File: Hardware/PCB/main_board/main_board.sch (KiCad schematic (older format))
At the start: 0 parts

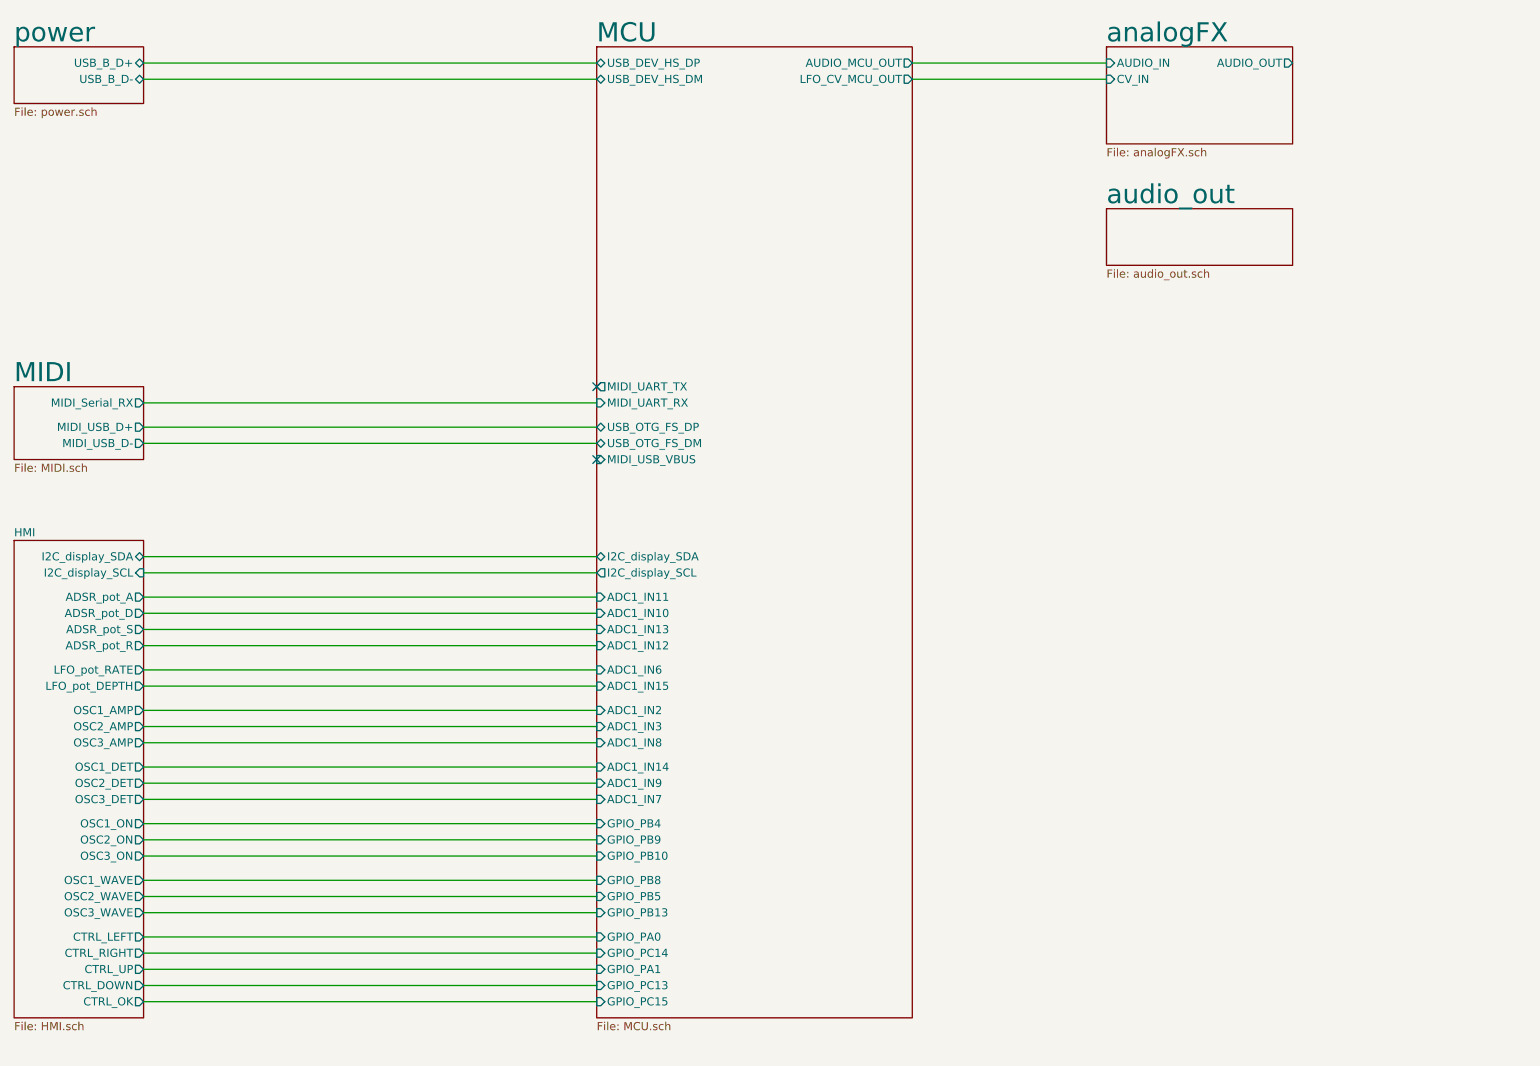
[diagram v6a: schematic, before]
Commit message: Add FX buffer and headphone amp to schematics
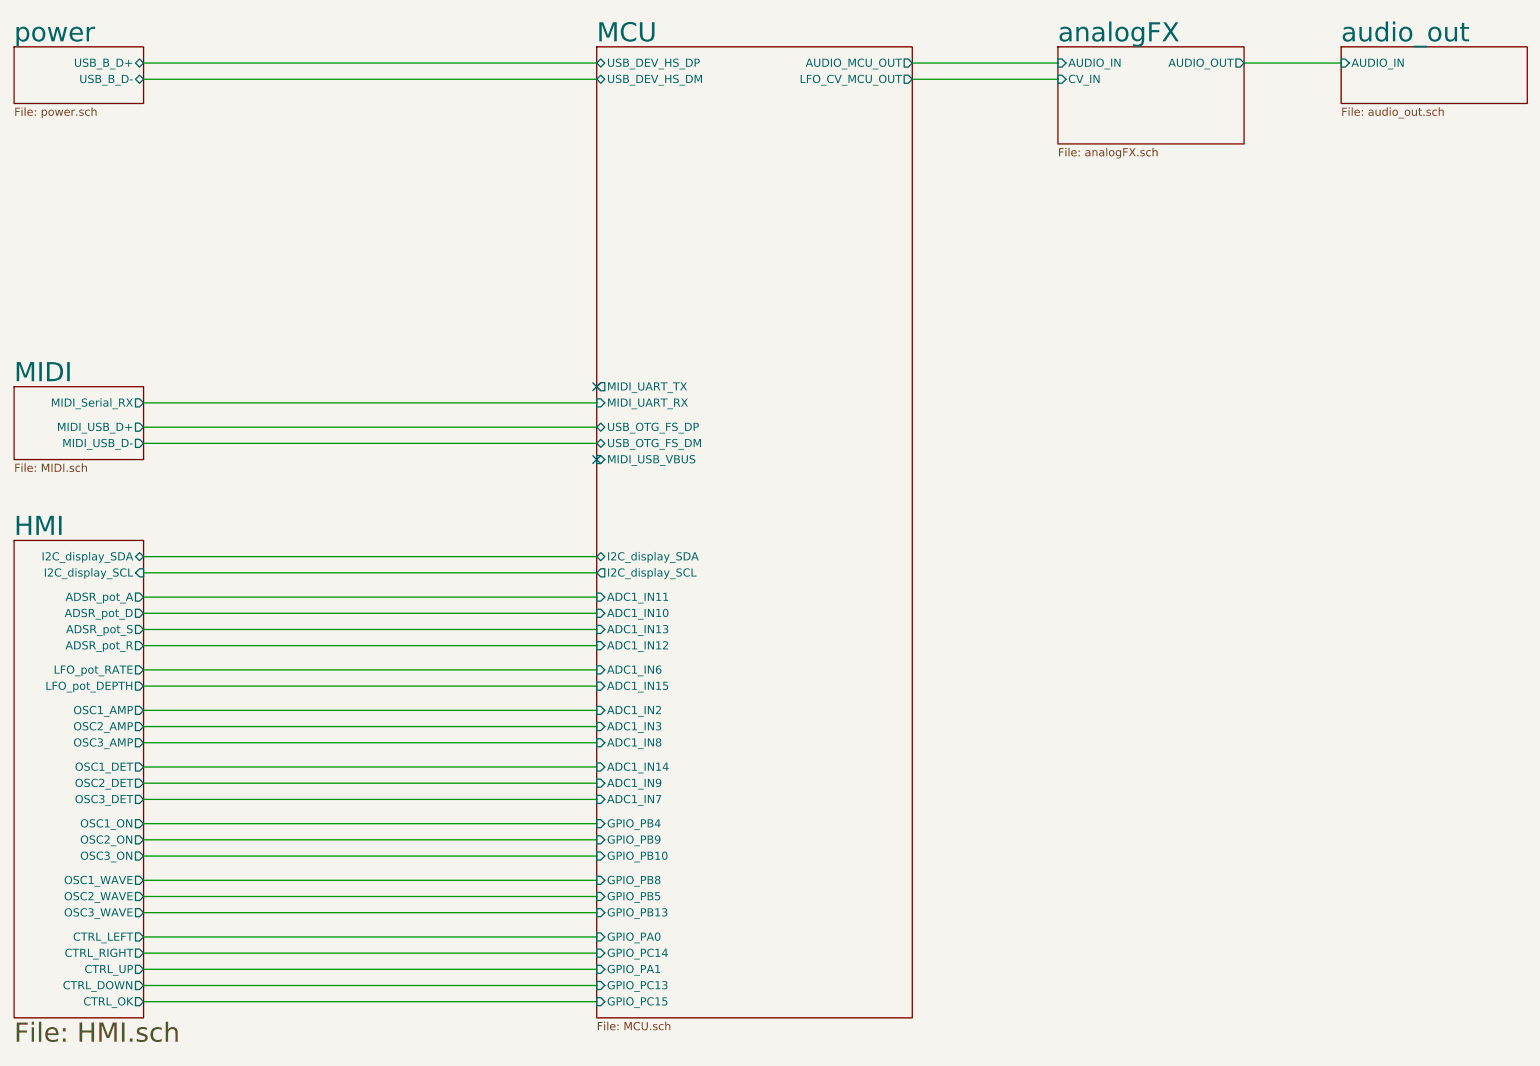
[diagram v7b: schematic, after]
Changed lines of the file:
@@
 $EndDescr
 Wire Wire Line
-	6750 1250 7950 1250
+	6750 1250 7650 1250
 Wire Wire Line
-	6750 1350 7950 1350
+	6750 1350 7650 1350
 $Sheet
 S 1200 3250 800  450
@@
 $EndSheet
 $Sheet
-S 7950 2150 1150 350
+S 9400 1150 1150 350
 U 5E68385C
 F0 "audio_out" 118
 F1 "audio_out.sch" 50
+F2 "AUDIO_IN" I L 9400 1250 50
 $EndSheet
 $Sheet
-S 7950 1150 1150 600
+S 7650 1150 1150 600
 U 5E632F77
 F0 "analogFX" 118
 F1 "analogFX.sch" 50
-F2 "AUDIO_OUT" O R 9100 1250 50
-F3 "CV_IN" I L 7950 1350 50
-F4 "AUDIO_IN" I L 7950 1250 50
+F2 "AUDIO_OUT" O R 8800 1250 50
+F3 "CV_IN" I L 7650 1350 50
+F4 "AUDIO_IN" I L 7650 1250 50
 $EndSheet
 $Sheet
 S 1200 4200 800  2950
 U 5E525BAF
-F0 "HMI" 50
-F1 "HMI.sch" 50
+F0 "HMI" 118
+F1 "HMI.sch" 118
 F2 "I2C_display_SDA" B R 2000 4300 50
 F3 "I2C_display_SCL" I R 2000 4400 50
@@
 Wire Wire Line
 	4800 1350 2000 1350
+Wire Wire Line
+	8800 1250 9400 1250
 $EndSCHEMATC

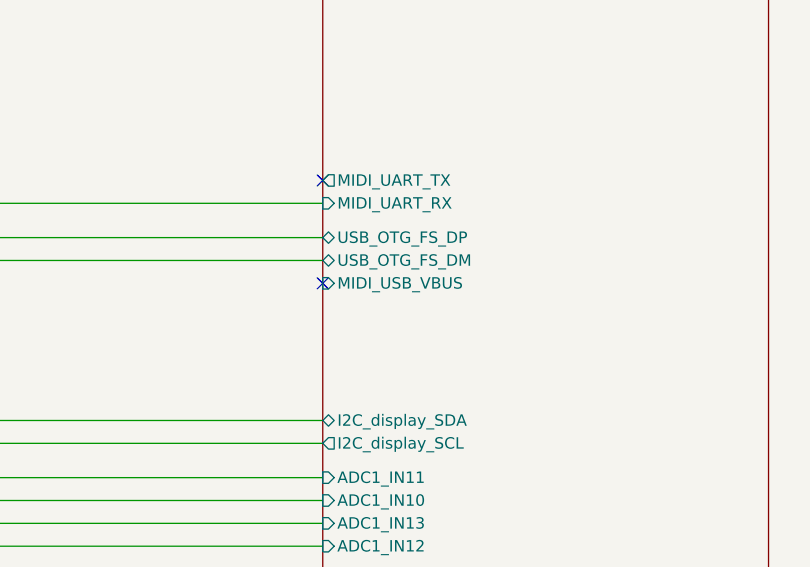
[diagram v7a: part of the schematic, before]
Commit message: Use bare STM32 instead of nucleo board. Schematics update
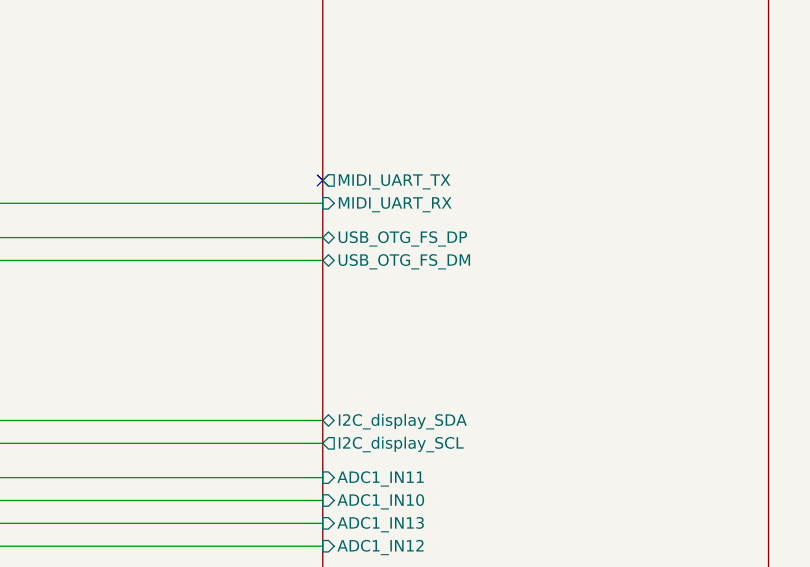
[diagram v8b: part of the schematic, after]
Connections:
- no-connect marks 2 -> 1
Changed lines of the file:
@@
 F8 "MIDI_UART_TX" O L 4800 3250 50
 F9 "MIDI_UART_RX" I L 4800 3350 50
-F10 "MIDI_USB_VBUS" I L 4800 3700 50
-F11 "ADC1_IN10" I L 4800 4650 50
-F12 "ADC1_IN11" I L 4800 4550 50
-F13 "ADC1_IN12" I L 4800 4850 50
-F14 "ADC1_IN13" I L 4800 4750 50
-F15 "ADC1_IN2" I L 4800 5250 50
-F16 "ADC1_IN3" I L 4800 5350 50
-F17 "ADC1_IN6" I L 4800 5000 50
-F18 "ADC1_IN7" I L 4800 5800 50
-F19 "ADC1_IN14" I L 4800 5600 50
-F20 "ADC1_IN15" I L 4800 5100 50
-F21 "ADC1_IN9" I L 4800 5700 50
-F22 "ADC1_IN8" I L 4800 5450 50
-F23 "GPIO_PA0" I L 4800 6650 50
-F24 "GPIO_PA1" I L 4800 6850 50
-F25 "GPIO_PC13" I L 4800 6950 50
-F26 "GPIO_PC14" I L 4800 6750 50
-F27 "GPIO_PC15" I L 4800 7050 50
-F28 "GPIO_PB13" I L 4800 6500 50
-F29 "GPIO_PB4" I L 4800 5950 50
-F30 "GPIO_PB5" I L 4800 6400 50
-F31 "GPIO_PB10" I L 4800 6150 50
-F32 "GPIO_PB8" I L 4800 6300 50
-F33 "GPIO_PB9" I L 4800 6050 50
-F34 "USB_DEV_HS_DM" B L 4800 1350 50
-F35 "USB_DEV_HS_DP" B L 4800 1250 50
+F10 "ADC1_IN10" I L 4800 4650 50
+F11 "ADC1_IN11" I L 4800 4550 50
+F12 "ADC1_IN12" I L 4800 4850 50
+F13 "ADC1_IN13" I L 4800 4750 50
+F14 "ADC1_IN2" I L 4800 5250 50
+F15 "ADC1_IN3" I L 4800 5350 50
+F16 "ADC1_IN6" I L 4800 5000 50
+F17 "ADC1_IN7" I L 4800 5800 50
+F18 "ADC1_IN14" I L 4800 5600 50
+F19 "ADC1_IN15" I L 4800 5100 50
+F20 "ADC1_IN9" I L 4800 5700 50
+F21 "ADC1_IN8" I L 4800 5450 50
+F22 "GPIO_PA0" I L 4800 6650 50
+F23 "GPIO_PA1" I L 4800 6850 50
+F24 "GPIO_PC13" I L 4800 6950 50
+F25 "GPIO_PC14" I L 4800 6750 50
+F26 "GPIO_PC15" I L 4800 7050 50
+F27 "GPIO_PB13" I L 4800 6500 50
+F28 "GPIO_PB4" I L 4800 5950 50
+F29 "GPIO_PB5" I L 4800 6400 50
+F30 "GPIO_PB10" I L 4800 6150 50
+F31 "GPIO_PB8" I L 4800 6300 50
+F32 "GPIO_PB9" I L 4800 6050 50
+F33 "USB_DEV_HS_DM" B L 4800 1350 50
+F34 "USB_DEV_HS_DP" B L 4800 1250 50
 $EndSheet
 Wire Wire Line
@@
 	2000 3350 4800 3350
 NoConn ~ 4800 3250
-NoConn ~ 4800 3700
 Wire Wire Line
 	2000 1250 4800 1250
